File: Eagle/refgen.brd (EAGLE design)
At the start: 111.1 x 72.4 mm, 23 parts, among them J1 USB-B

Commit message: Finished up chanes to DB25
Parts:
- removed C10: 1uF, resistor:E5-8,5
- removed C11, C12, C14: 0.1uF, resistor:C050-025X075
- removed C13: 0.01uF, resistor:C050-025X075
- removed C15: 47uF, resistor:E5-8,5
- removed CN1: (no value), adafruit:DCJACK_2MM_PTH
- removed D1: 1N5818-B, diode:DO41-7.6
- removed J1: USB-B, SparkFun-Connectors:USB-B-PTH
- removed JP1: (no value), jumper:JP1
- removed L1: BL02RN1, inductors:BL02RN1
- removed LED1: (no value), led:LED3MM
- removed U$1: PIC18F4458, PIC18:DIL40
- removed U$2: PIC-ICSPPOLAR_LOCK, SparkFun-Connectors:MOLEX-1X6_LOCK
- removed U$3: ROL-0505S, modEEG:SIP4
- removed Y1: (no value), SparkFun-FreqCtrl:HC49US
- added C6: 1nF, resistor:C050-025X075
- added C7, C8, C9: 0.01uf, resistor:C050-025X075
- added IC1: (no value), BURR:DIL-08
- added IC2: MAX6341N, EEG:DIL08
- added MON_RLD, MON_VREF: BNCPTH, SparkFun-Connectors:BNC
- added R1: (no value), resistor:0204V
- added R2, R4: (no value), resistor:RTRIM3296W
- added R5: 200k, resistor:0204V
- added RLD_COM, RLD_OUT, VCOM: TPPAD1-17, testpad:P1-17
- C1, C2: value (none) -> 0.01uf
- C3: value 0.47uF -> 0.1uf
- C4: value 0.1uF -> 0.1uf
- C5: value 0.1uF -> 1nF
- R3: value 200k -> (none)
- X1: device con-subd:M25H -> con-subd:M25HP
- moved R3 66.5 mm to (67.3, 26.7), turned to 0 degrees
- moved C5 35.3 mm to (19.1, 58.4), turned to 180 degrees
- moved C4 32.8 mm to (69.8, 44.5), turned to 90 degrees
- moved C2 22.2 mm to (63.5, 31.8), turned to 0 degrees
- moved C3 19.1 mm to (69.8, 36.8), turned to 90 degrees
- moved C1 17.1 mm to (50.8, 21.6), turned to 270 degrees
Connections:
- removed net +5V/2: C10.+, C11.1, C3.1, C4.1, C5.1, CN1.PWR, D1.C, JP1.2, U$1.11, U$1.32, U$3.P$2
- removed net CNV: U$1.25, X1.19
- removed net DGND: C1.1, C10.-, C11.2, C2.1, C4.2, C5.2, CN1.GND, D1.A, J1.GND, U$1.12, U$1.31, U$2.4, U$3.P$1
- removed net GNDBREAK: CN1.GNDBREAK
- removed net N$10: JP1.1, U$2.5
- removed net N$11: U$1.37, X1.13
- removed net N$12: U$1.36, X1.25
- removed net N$13: U$1.35, X1.12
- removed net N$14: U$1.34, X1.24
- removed net N$15: U$1.30, X1.11
- removed net N$16: U$1.29, X1.23
- removed net N$17: U$1.28, X1.10
- removed net N$18: U$1.27, X1.22
- removed net N$19: U$1.22, X1.9
- removed net N$20: U$1.21, X1.21
- removed net N$26: C12.1, L1.2, R3.2, U$3.P$4
- removed net N$28: LED1.A, R3.1
- removed net N$7: U$1.39, U$2.2
- removed net N$8: U$1.40, U$2.3
- removed net N$9: C3.2, U$1.18
- removed net RD0: U$1.19, X1.8
- removed net RD1: U$1.20, X1.20
- removed net SCK: U$1.26, X1.7
- new net RLD_COM: C6.1, IC1.6, RLD_COM.TP, X1.15
- new net VCOM: C3.2, C4.1, C7.2, C8.1, IC1.1, IC1.2, MON_RLD.GND, MON_VREF.GND, R4.3, VCOM.TP, X1.2, X1.5
- new net VREF: C1.1, IC2.6, MON_VREF.S, R1.1, X1.3
- net +5V: now also C3.1, C7.1, C9.1, IC1.8, IC2.2; no longer C13.1, C14.1, C15.+, L1.1
- net GND: now also C1.2, C2.2, C4.2, C8.2, C9.2, IC1.4, IC2.4, R3.2, R4.1; no longer C12.2, C13.2, C14.2, C15.-, LED1.K, U$3.P$3
- net N$1: now also C5.1, IC1.7, R5.1; no longer C1.2, U$1.14, Y1.2
- net N$2: now also R1.2, R2.3; no longer C2.2, U$1.13, Y1.1
- net N$3: now also R2.1, R3.1; no longer J1.D+, U$1.24
- net N$4: now also C2.1, IC1.3, R2.2; no longer J1.D-, U$1.23
- net N$5: now also C5.2, C6.2, MON_RLD.S, R5.2, RLD_OUT.TP; no longer U$1.1, U$2.6
- net N$6: now also IC1.5, R4.2; no longer U$1.38, U$2.1
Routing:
- net DGND: track 170.5 -> 0.00 mm, vias 2 -> 0
- net VCOM: track 0.00 -> 160.0 mm, vias 0 -> 1
- net +5V/2: track 113.8 -> 0.00 mm
- net RLD_COM: track 0.00 -> 110.5 mm
- net VREF: track 0.00 -> 99.1 mm
- net N$11: track 73.3 -> 0.00 mm
- net N$12: track 72.8 -> 0.00 mm
- net N$13: track 67.1 -> 0.00 mm
- net N$14: track 66.5 -> 0.00 mm
- net N$3: track 70.1 -> 3.81 mm
- net N$4: track 70.0 -> 16.1 mm
- net N$15: track 50.3 -> 0.00 mm
- net N$16: track 49.7 -> 0.00 mm
- net N$5: track 28.6 -> 77.7 mm
- net N$26: track 48.4 -> 0.00 mm
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- added copper zone on layer 16, net VCOM
- removed copper zone on layer 16, net GND

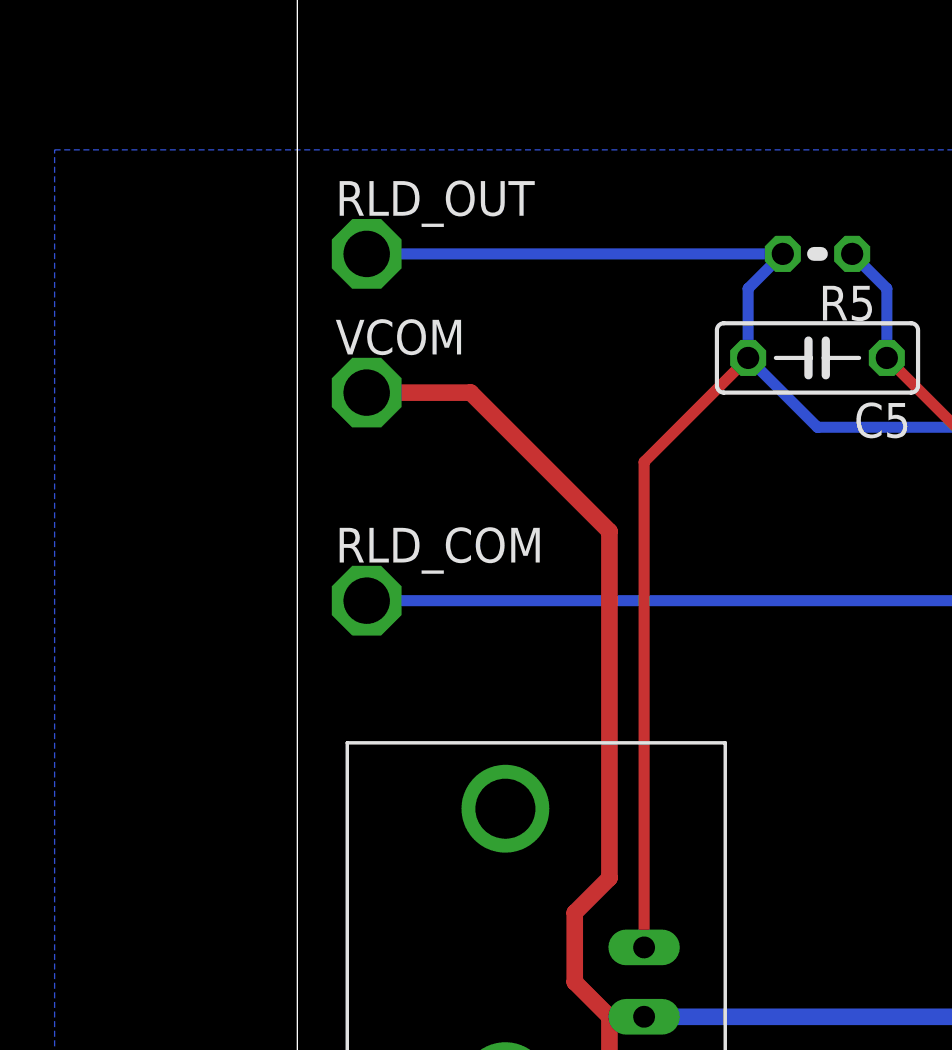
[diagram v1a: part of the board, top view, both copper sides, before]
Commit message: Added DIN 42802 jacks & power for active electrodes
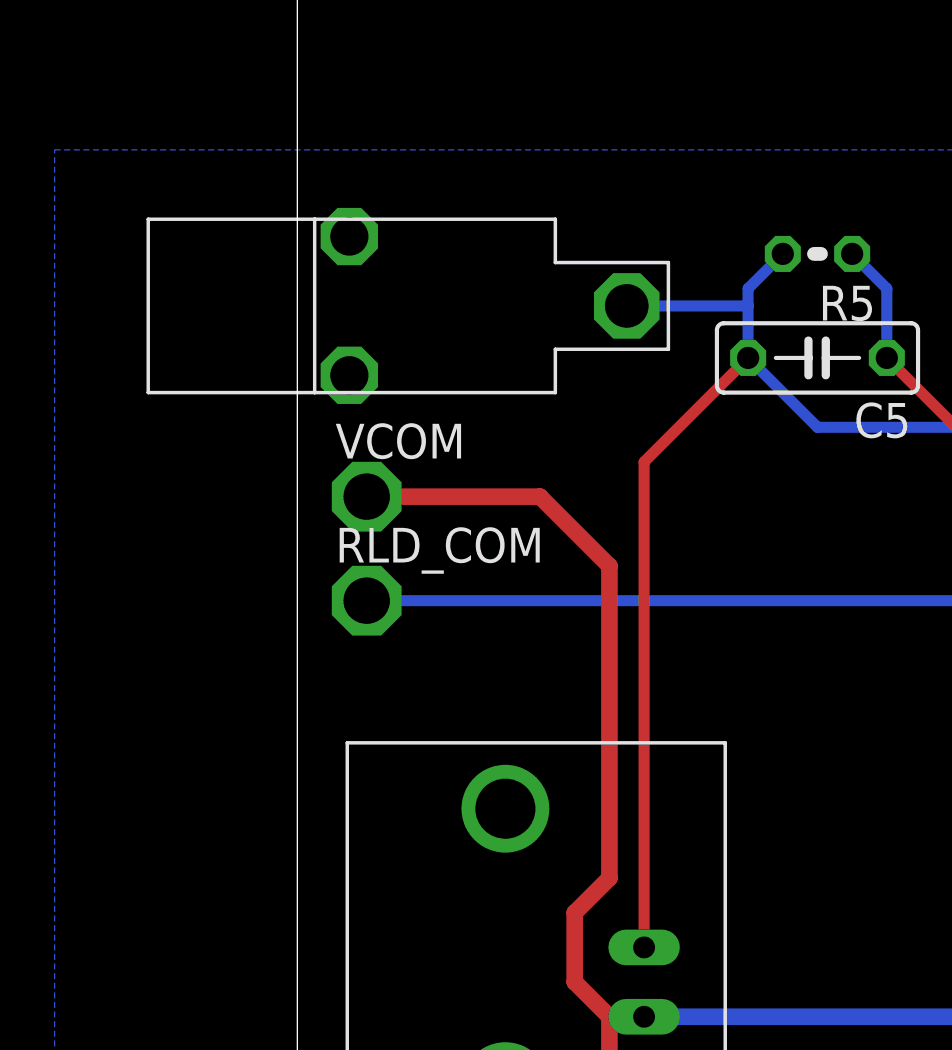
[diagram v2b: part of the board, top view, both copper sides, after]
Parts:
- RLD_OUT: value TPPAD1-17 -> DIN42802; device testpad:P1-17 -> modEEG:DIN42802
- moved VCOM 3.81 mm to (2.54, 53.3)
- moved RLD_OUT 2.01 mm to (1.91, 60.3), turned to 90 degrees
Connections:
- net N$5: now also RLD_OUT.P$1; no longer RLD_OUT.TP
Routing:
- net N$5: track 77.7 -> 66.9 mm
- net VCOM: track 160.0 -> 157.6 mm
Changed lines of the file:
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@@
 <element name="R4" library="resistor" package="RTRIM3296W" value="" x="52.07" y="49.53" rot="R90"/>
 <element name="R5" library="resistor" package="0204V" value="200k" x="19.05" y="62.23" rot="R180"/>
-<element name="RLD_OUT" library="testpad" package="P1-17" value="TPPAD1-17" x="2.54" y="62.23">
-<attribute name="TP_SIGNAL_NAME" value="" x="2.54" y="62.23" size="1.778" layer="27" display="off"/>
-</element>
-<element name="VCOM" library="testpad" package="P1-17" value="TPPAD1-17" x="2.54" y="57.15">
-<attribute name="TP_SIGNAL_NAME" value="" x="2.54" y="57.15" size="1.778" layer="27" display="off"/>
+<element name="VCOM" library="testpad" package="P1-17" value="TPPAD1-17" x="2.54" y="53.34">
+<attribute name="TP_SIGNAL_NAME" value="" x="2.54" y="53.34" size="1.778" layer="27" display="off"/>
 </element>
 <element name="X1" library="con-subd" package="M25HP" value="" x="100.33" y="36.83" rot="R90">
@@
 </element>
 <element name="C9" library="resistor" package="C050-025X075" value="0.01uf" x="44.45" y="20.32"/>
+<element name="RLD_OUT" library="modEEG" package="DIN42802" value="DIN42802" x="1.905" y="60.325" rot="R90"/>
 </elements>
 <signals>
@@
 <vertex x="-8.89" y="5.08"/>
 </polygon>
-<wire x1="2.54" y1="57.15" x2="6.35" y2="57.15" width="0.6096" layer="1"/>
-<wire x1="6.35" y1="57.15" x2="11.43" y2="52.07" width="0.6096" layer="1"/>
-<wire x1="11.43" y1="52.07" x2="11.43" y2="39.37" width="0.6096" layer="1"/>
+<wire x1="2.54" y1="53.34" x2="8.89" y2="53.34" width="0.6096" layer="1"/>
+<wire x1="8.89" y1="53.34" x2="11.43" y2="50.8" width="0.6096" layer="1"/>
+<wire x1="11.43" y1="50.8" x2="11.43" y2="39.37" width="0.6096" layer="1"/>
 <wire x1="11.43" y1="39.37" x2="10.16" y2="38.1" width="0.6096" layer="1"/>
 <wire x1="10.16" y1="38.1" x2="10.16" y2="35.56" width="0.6096" layer="1"/>
@@
 <contactref element="R5" pad="2"/>
 <contactref element="C6" pad="2"/>
-<contactref element="RLD_OUT" pad="TP"/>
 <contactref element="MON_RLD" pad="S"/>
-<wire x1="2.54" y1="62.23" x2="17.78" y2="62.23" width="0.4064" layer="16"/>
-<wire x1="16.51" y1="58.42" x2="16.51" y2="60.96" width="0.4064" layer="16"/>
+<wire x1="16.51" y1="58.42" x2="16.51" y2="60.325" width="0.4064" layer="16"/>
+<wire x1="16.51" y1="60.325" x2="16.51" y2="60.96" width="0.4064" layer="16"/>
 <wire x1="16.51" y1="60.96" x2="17.78" y2="62.23" width="0.4064" layer="16"/>
 <wire x1="45.72" y1="44.45" x2="34.29" y2="55.88" width="0.4064" layer="16"/>
@@
 <wire x1="12.7" y1="36.83" x2="12.7" y2="54.61" width="0.4064" layer="1"/>
 <wire x1="12.7" y1="54.61" x2="16.51" y2="58.42" width="0.4064" layer="1"/>
+<contactref element="RLD_OUT" pad="P$1"/>
+<wire x1="12.065" y1="60.325" x2="16.51" y2="60.325" width="0.4064" layer="16"/>
 </signal>
 <signal name="N$6">

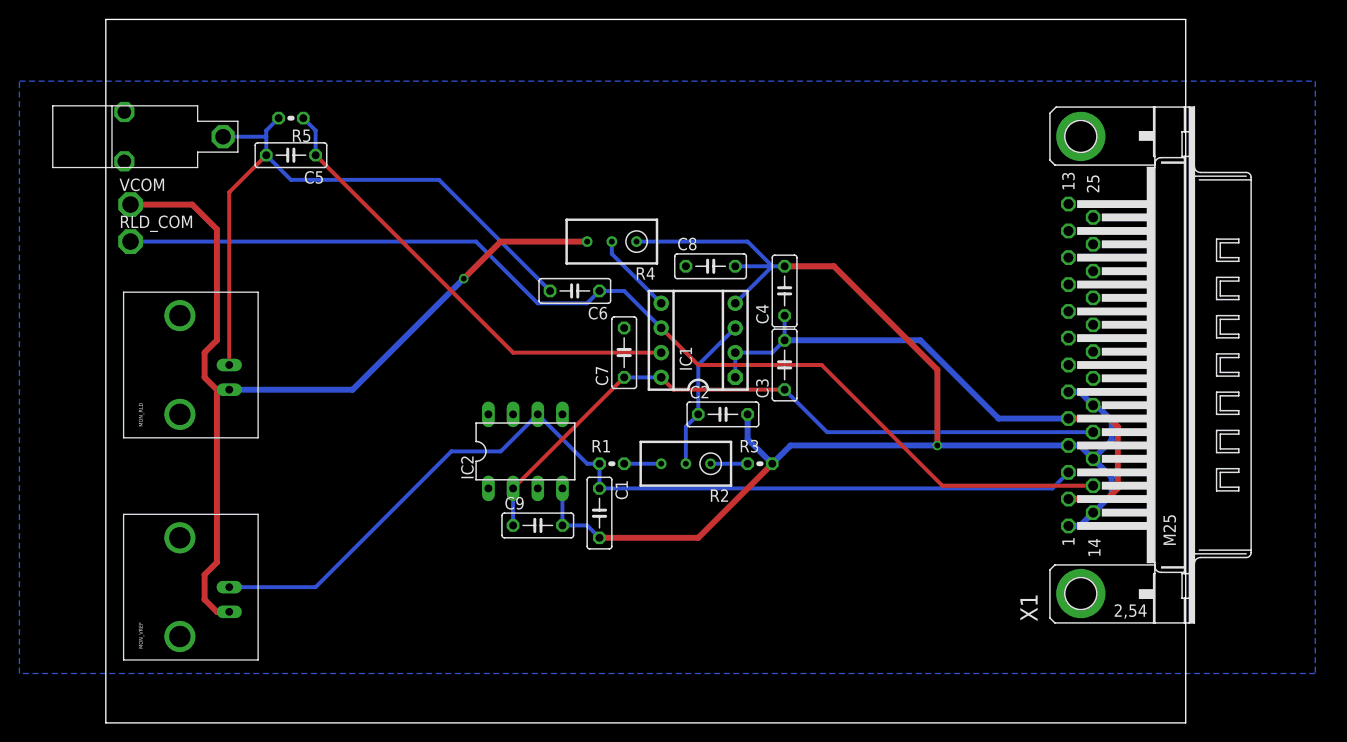
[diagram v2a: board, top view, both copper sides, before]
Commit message: Board shrink
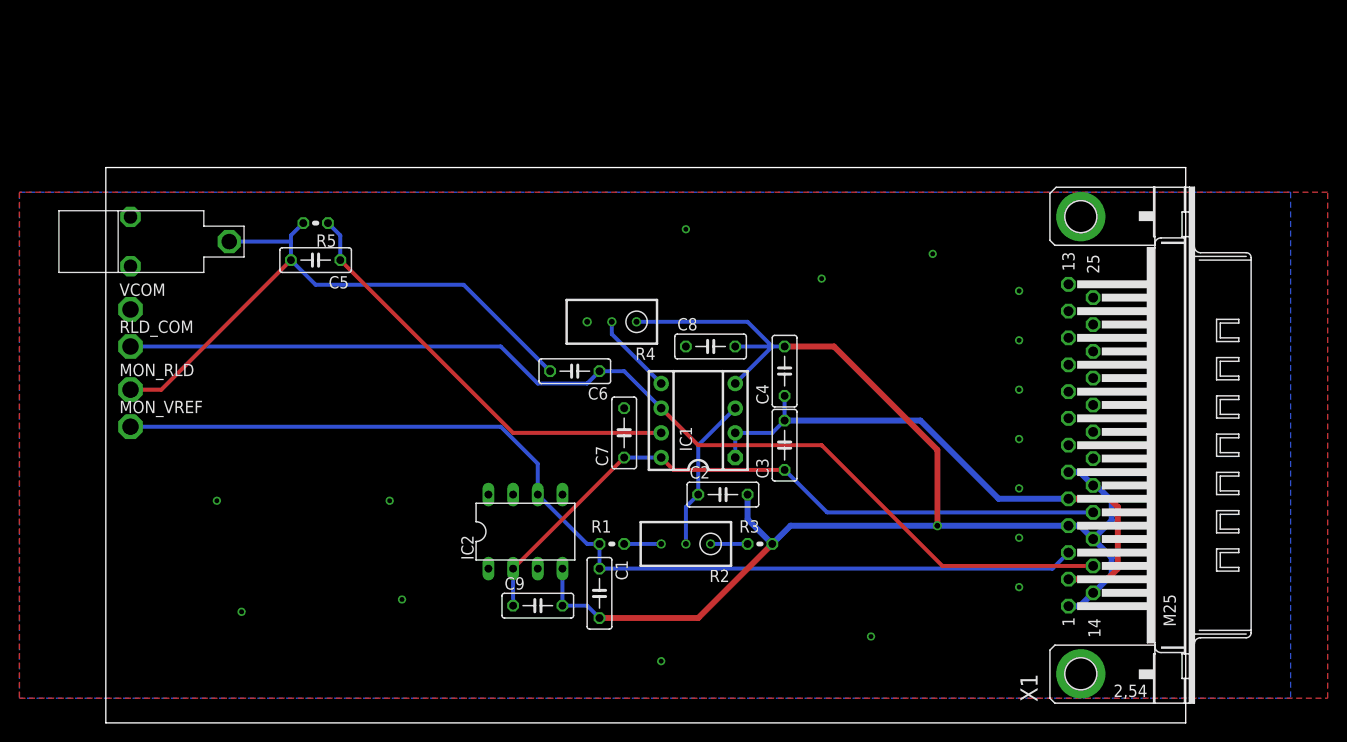
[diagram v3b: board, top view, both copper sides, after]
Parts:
- C1, C9: value 0.01uf -> 2.2uF
- MON_RLD, MON_VREF: value BNCPTH -> TPPAD1-17; device SparkFun-Connectors:BNC -> testpad:P1-17
- moved MON_VREF 19.4 mm to (2.54, 30.5), turned to 0 degrees
- moved C5 11.1 mm to (21.6, 47.6)
- moved R5 11.1 mm to (21.6, 51.4)
- moved RLD_OUT 10.8 mm to (2.54, 49.5)
- moved RLD_COM 10.8 mm to (2.54, 38.7)
- moved VCOM 10.8 mm to (2.54, 42.5)
- moved MON_RLD 10.5 mm to (2.54, 34.3), turned to 0 degrees
- moved C4 8.26 mm to (69.8, 36.2)
- moved C6 8.26 mm to (48.3, 36.2)
- moved C7 8.26 mm to (53.3, 29.8)
- moved C8 8.26 mm to (62.2, 38.7)
- moved IC2 8.26 mm to (43.2, 19.7)
- moved R1 8.26 mm to (52.1, 18.4)
- moved R2 8.26 mm to (59.7, 18.4)
- moved R3 8.26 mm to (67.3, 18.4)
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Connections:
- net N$5: now also MON_RLD.TP; no longer MON_RLD.S
- net VCOM: no longer MON_RLD.GND, MON_VREF.GND
- net VREF: now also MON_VREF.TP; no longer MON_VREF.S
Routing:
- net VCOM: track 157.6 -> 60.5 mm, vias 1 -> 16
- net VREF: track 99.1 -> 106.6 mm
- net N$1: track 48.3 -> 44.7 mm
- net N$5: track 66.9 -> 64.1 mm
- net RLD_COM: track 110.5 -> 109.5 mm
- added copper zone on layer 1, net VCOM
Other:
- board size 111.1 x 72.4 mm -> 111.1 x 57.1 mm
